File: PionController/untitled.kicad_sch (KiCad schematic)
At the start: 2 parts

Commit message: Power_Fix
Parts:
- removed C1: 10uF, Capacitor_SMD:C_1210_3225Metric, symbol Device:C
- added C1, C11, C2, C3, C4, C7, C8: 10uF, Capacitor_SMD:C_1210_3225Metric, symbol Device:C_Small
- added C10, C9: 2.2uF, symbol Device:C_Small
- added C5, C6: 100nF, Capacitor_SMD:C_0805_2012Metric, symbol Device:C_Small
- added CMC1: PSMCAQ1050-801P, Inductor_SMD:L_CommonModeChoke_Wuerth_WE-SL5, symbol Device:L_Ferrite_Coupled_1423
- added L1: 33uH, Inductor_SMD:L_TDK_SLF10145, symbol Device:L_Ferrite
- added L2: 4.7uH, Inductor_SMD:L_0603_1608Metric, symbol Device:L_Ferrite_Small
- added R1: 54.9K, Resistor_SMD:R_0805_2012Metric, symbol Device:R_Small
- added R2, R3: 10K, Resistor_SMD:R_0805_2012Metric, symbol Device:R_Small
- added U2: TLV75733PDBV, Package_TO_SOT_SMD:SOT-23-5, symbol Regulator_Linear:TLV75733PDBV
- added Ue1: TPS562200, Package_TO_SOT_SMD:SOT-23-6, symbol Regulator_Switching:TPS562200
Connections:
- net +12V_CAR: now also D1.1 (A1), C2.1, L1.1
- net GND_CAR: now also D1.2 (A2), C1.2, C2.2, CMC1.1
- new net: C1.1, CMC1.2, L1.2
- new net: R1.2, R2.1, Ue1.4 (VFB)
- new net: C6.2, L2.1, Ue1.2 (SW)
- new net: R3.2, U2.3 (EN)
- new net: C6.1, Ue1.6 (VBST)
- new net +12V: C11.1, C3.1, C4.1, C5.1, CMC1.3, Ue1.3 (VIN), Ue1.5 (EN)
- new net +3.3V: C10.1, U2.5 (OUT)
- new net +5V: C7.1, C8.1, C9.1, L2.2, R1.1, R3.1, U2.1 (IN)
- new net GND: C10.2, C11.2, C3.2, C4.2, C5.2, C7.2, C8.2, C9.2, CMC1.4, R2.2, U2.2 (GND), Ue1.1 (GND)
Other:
- note added: "12V to 5V Regulator"
- note added: "5V to 3.3V Regulator"
- note added: "ESD PROTECTION"
- moved on the sheet: D1

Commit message: Schematic_ready
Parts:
- C10, C9: footprint (none) -> Capacitor_SMD:C_0603_1608Metric; LCSC (none) -> C914769; Manufacturer (none) -> CC0603KRX7R7BB225
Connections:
- net GND_CAR is gone; now on net GND: C1.2, C2.2, CMC1.1, D1.2 (A2)
- net +3.3V: now also C10.2; no longer C10.1
- net +5V: now also C9.2; no longer C9.1
- net GND: now also C10.1, C9.1; no longer C10.2, C9.2

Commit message: Version 1
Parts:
- removed C2: 10uF, Capacitor_SMD:C_1210_3225Metric, symbol Device:C_Small
- removed L1: 33uH, Inductor_SMD:L_TDK_SLF10145, symbol Device:L_Ferrite
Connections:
- net +12V_CAR: now also C1.1, CMC1.2
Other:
- moved on the sheet: C1, C11, CMC1

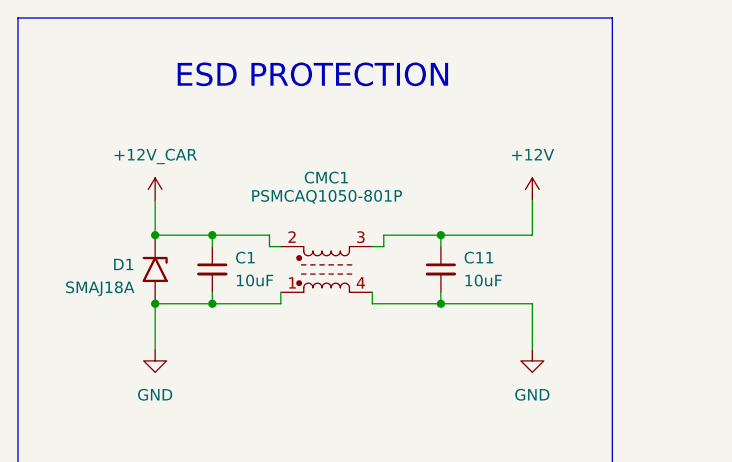
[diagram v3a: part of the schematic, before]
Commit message: Librery fix, 3d models added and fiducial marks
Library Fix: Added missing components and updated footprints, ensuring all parts are properly referenced.
3D Models Added: Integrated 3D models for visual reference in the PCB layout and to assist with mechanical fitment checks.
Fiducial Marks: Placed fiducial marks on the board for accurate alignment during automated assembly processes.
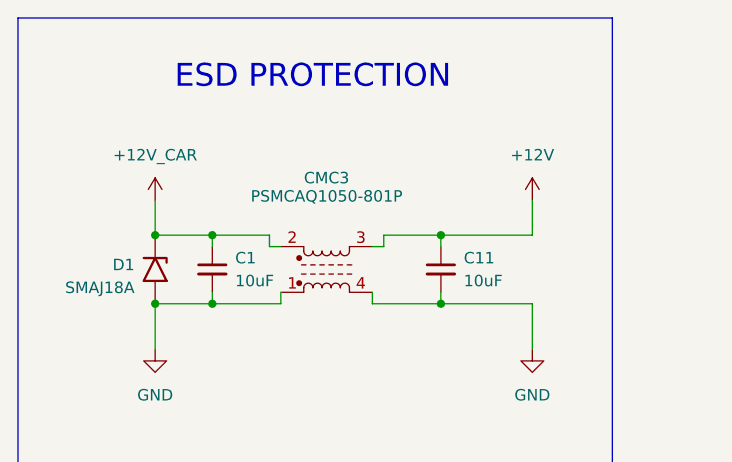
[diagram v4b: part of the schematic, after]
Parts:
- D1: LCSC (none) -> C148219; Manufacturer (none) -> SMAJ18A
- renumbered CMC1 to CMC3
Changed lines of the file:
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@@
+			)
+		)
+		(property "Comment" ""
+			(at 57.15 96.52 0)
+			(effects
+				(font
+					(size 1.27 1.27)
+				)
+				(hide yes)
 			)
 		)
@@
 		(on_board yes)
 		(dnp no)
-		(property "Reference" "CMC1"
+		(property "Reference" "CMC3"
 			(at 55.88 35.56 0)
 			(effects
@@
 			(project "PionController"
 				(path "/4c75befe-3f28-4e3b-aaa6-2731a1e568ad/9c944e10-f70f-4daf-a172-373cee634d1f"
-					(reference "CMC1")
+					(reference "CMC3")
 					(unit 1)
 				)
@@
 			)
 		)
+		(property "LCSC" "  C148219"
+			(at 36.83 45.72 0)
+			(effects
+				(font
+					(size 1.27 1.27)
+				)
+				(hide yes)
+			)
+		)
+		(property "Manufacturer" "  SMAJ18A"
+			(at 36.83 45.72 0)
+			(effects
+				(font
+					(size 1.27 1.27)
+				)
+				(hide yes)
+			)
+		)
+		(property "Comment" ""
+			(at 36.83 45.72 0)
+			(effects
+				(font
+					(size 1.27 1.27)
+				)
+				(hide yes)
+			)
+		)
 		(pin "1"
 		)
@@
 			(at 173.99 104.14 0)
 			(effects
+				(font
+					(size 1.27 1.27)
+				)
+				(hide yes)
+			)
+		)
+		(property "Comment" ""
+			(at 173.99 104.14 0)
+			(effects
